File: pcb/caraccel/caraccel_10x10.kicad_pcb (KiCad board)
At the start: 2 copper layers, 100 x 100 mm, 7 parts, among them J1 LESP, J2 RESP

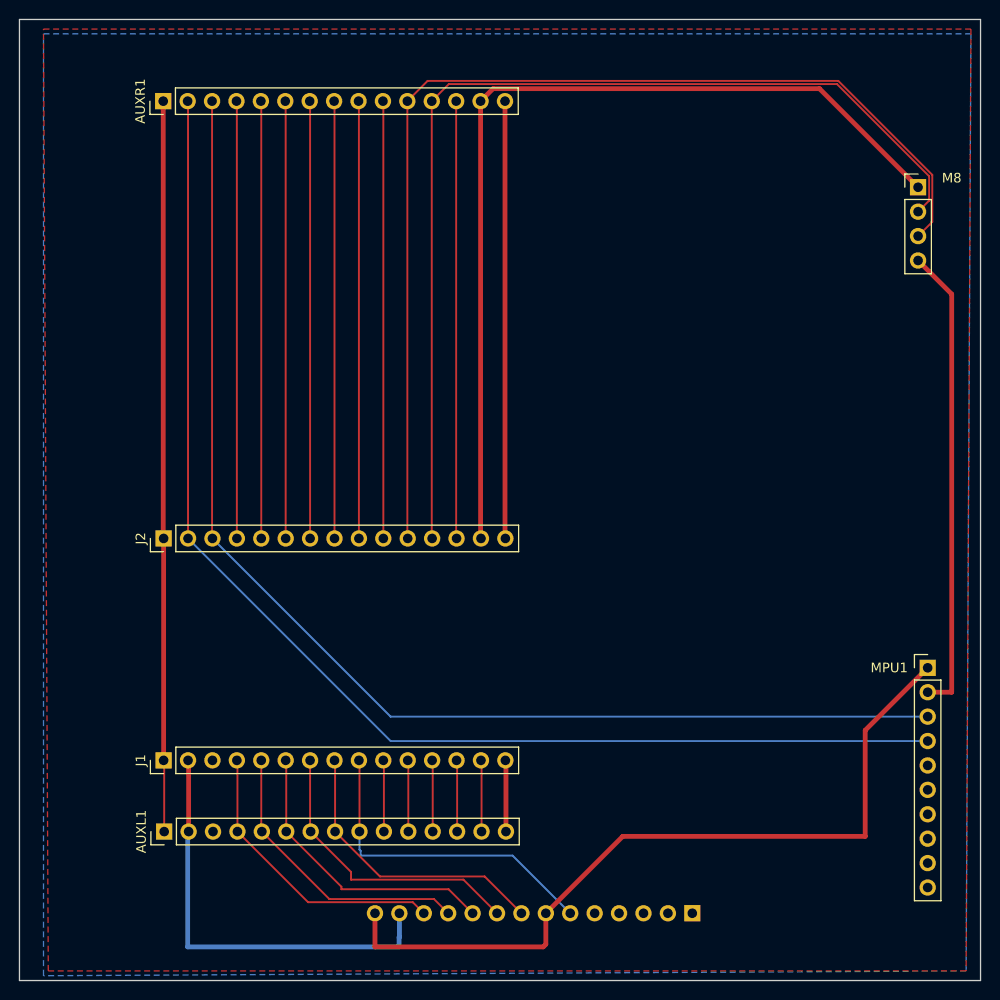
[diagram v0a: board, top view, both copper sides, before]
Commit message: Fixed space in PCB 10x10 for ESP-C6. 1 inch instead of 0.9
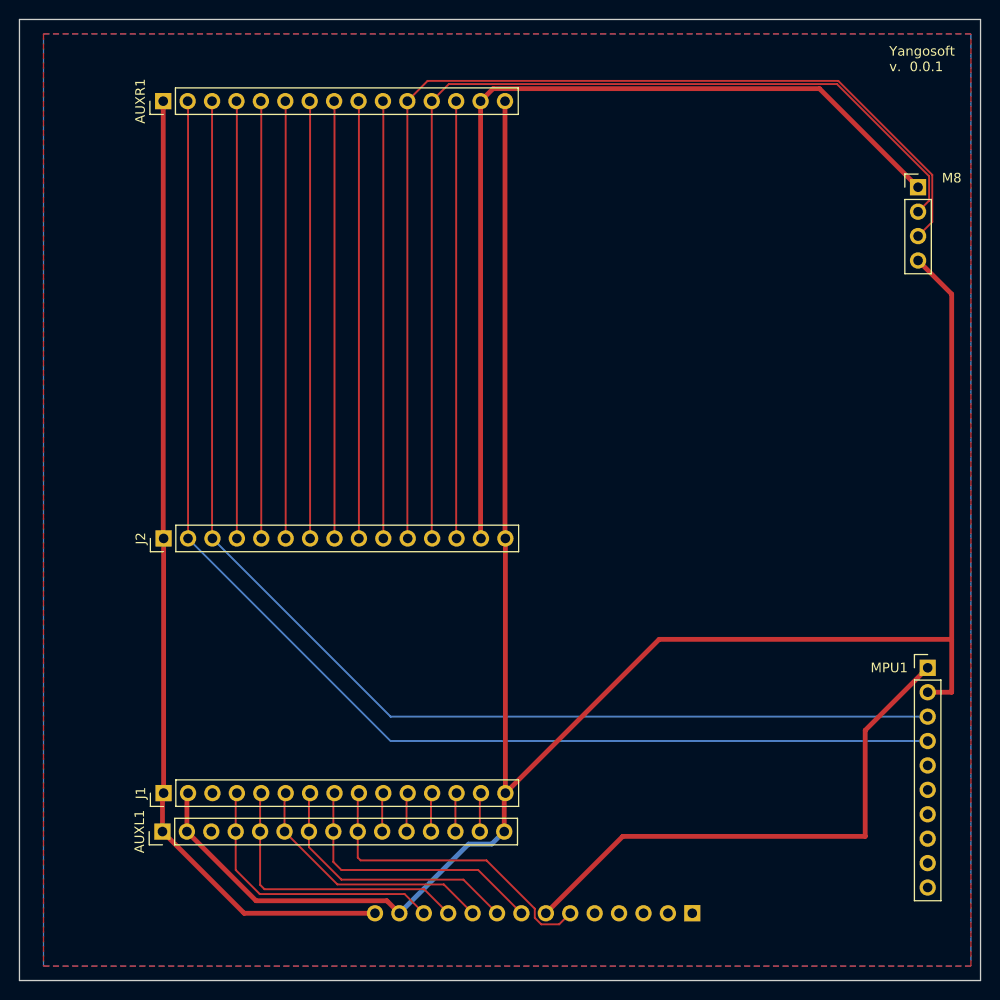
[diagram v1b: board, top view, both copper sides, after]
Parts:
- moved J1 3.41 mm to (124.5, 109.0)
- moved AUXL1 0.18 mm to (124.4, 113.0)
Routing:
- net GND: track 146.9 -> 222.1 mm
- net Net-(AUXL1-Pin_14): track 7.49 -> 4.05 mm
- net Net-(AUXL1-Pin_13): track 7.49 -> 4.05 mm
- net Net-(AUXL1-Pin_10): track 7.49 -> 4.05 mm
- net Net-(AUXL1-Pin_12): track 7.49 -> 4.05 mm
- net Net-(AUXL1-Pin_11): track 7.49 -> 4.05 mm
- net /DC: track 30.6 -> 27.1 mm
- net /MOSI: track 30.9 -> 28.1 mm
- net /MISO: track 34.3 -> 32.8 mm
- net /SLK: track 30.4 -> 29.0 mm
- net +5V: track 157.5 -> 158.5 mm
- net /CS: track 30.4 -> 29.5 mm
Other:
- board text added: "CAR ACCEL"
- board text added: "Yangosoft v. 0.0.1"

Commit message: Changes in PCB
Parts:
- moved TFT1 32.1 mm to (147.4, 121.5), turned to -90 degrees
- moved MPU1 22.6 mm to (203.5, 118.6), turned to 180 degrees
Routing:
- net GND: track 222.1 -> 80.1 mm
- net /SDA: track 131.2 -> 45.5 mm
- net +5V: track 158.5 -> 76.1 mm
- net /SCL: track 127.6 -> 45.5 mm
- net /MISO: track 32.8 -> 4.05 mm
- net /RST: track 30.4 -> 4.05 mm
- net /CS: track 29.5 -> 4.05 mm
- net /SLK: track 29.0 -> 4.05 mm
- net /MOSI: track 28.1 -> 4.05 mm
- net /DC: track 27.1 -> 4.05 mm
- removed copper zone on F.Cu, net +5V
- removed copper zone on B.Cu, net GND
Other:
- board text added: "3v3"
- board text added: "5v"
- board text added: "GND"
- board text added: "Yangosoft v. 0.1.0"
- board text added: "Yangosoft v. 0.2.0"
- board text removed: "Yangosoft v. 0.0.1"
